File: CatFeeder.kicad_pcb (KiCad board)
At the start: 2 copper layers, 96.3 x 51.8 mm, 49 parts, among them J1 B2B-XH-A(LF)(SN), J10 B2B-XH-A(LF)(SN), J11 B2B-XH-A(LF)(SN), J2 B3B-XH-A(LF)(SN), J3 Barrel_Jack, J4 B4B-XH-A(LF)(SN), J5 Conn_01x08_Female, J6 Conn_01x08_Female, J7 B2B-XH-A(LF)(SN), J8 B2B-XH-A(LF)(SN), J9 B2B-XH-A(LF)(SN), Q1 Q_NPN_BEC, Q2 Q_NPN_BEC, U1 SN74LVC1T45DBV, U2 LM2586SX-ADJ/NOPB_1, U3 DRV8871DDA

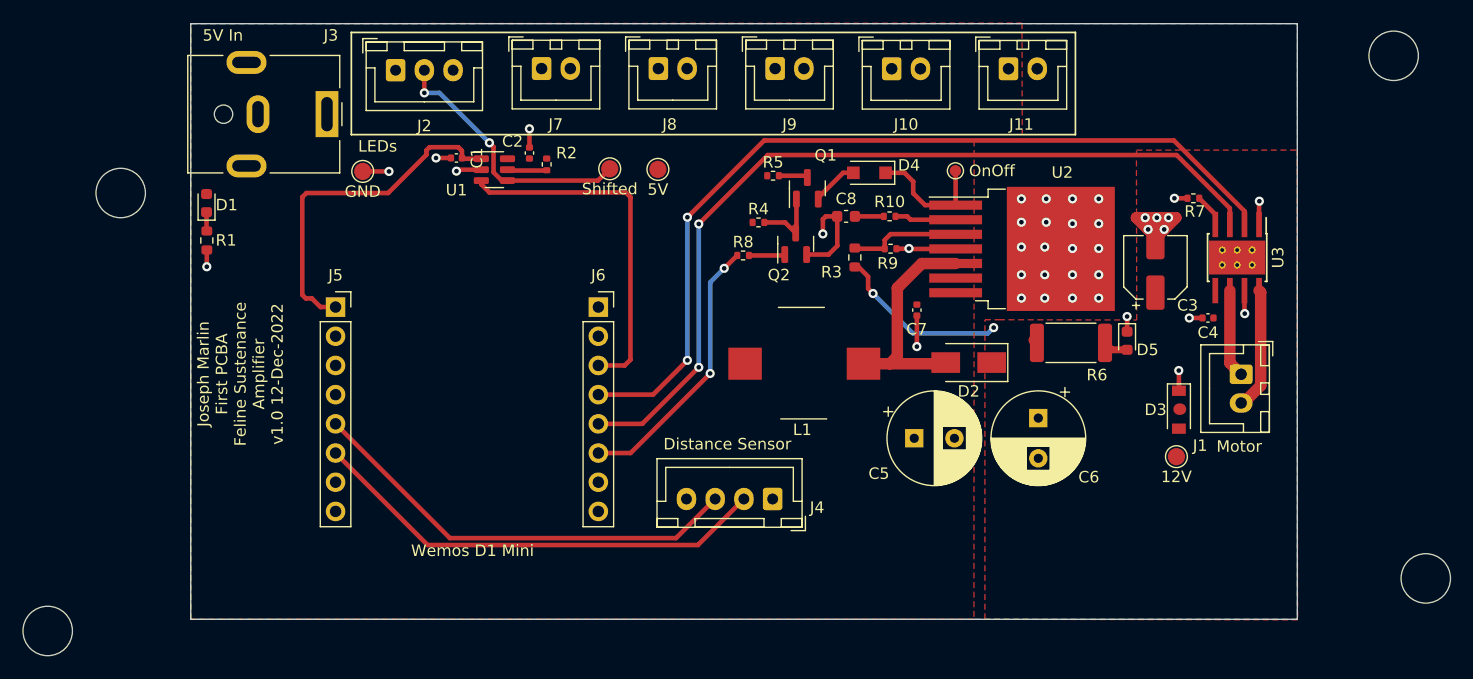
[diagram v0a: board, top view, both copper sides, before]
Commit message: Add pull ups to signals, tweak layout, reduce board size, add mounting holes
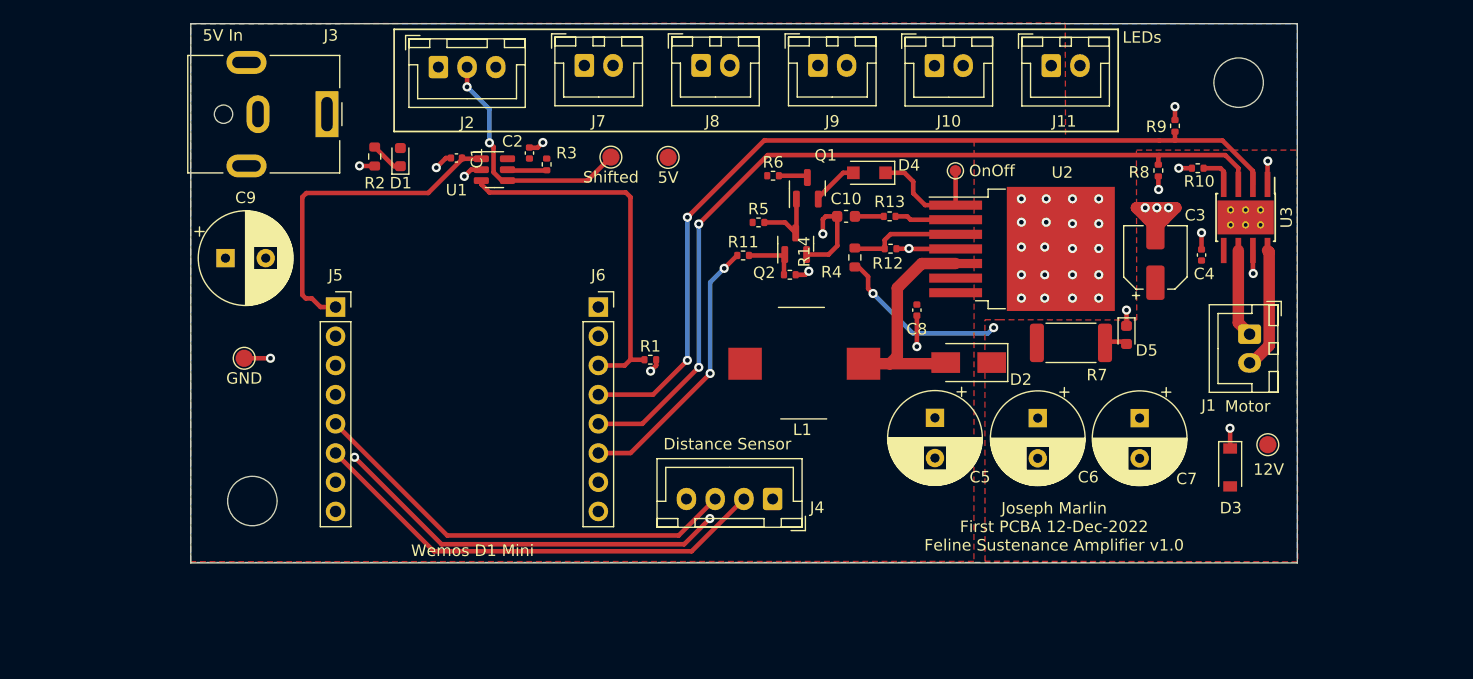
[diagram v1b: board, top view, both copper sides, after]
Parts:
- removed the REF** at (85.1, 120.9)
- removed the REF** at (205.0, 116.3)
- added C7: 680uF 25V, Capacitor_THT:CP_Radial_D8.0mm_P3.50mm, F.Cu at (180.1, 102.4)
- added C9: 100uF 25V, Capacitor_THT:CP_Radial_D8.0mm_P3.50mm, F.Cu at (100.6, 88.5)
- added R1: 30K, Resistor_SMD:R_0402_1005Metric, F.Cu at (137.5, 97.3)
- added R14: 30K, Resistor_SMD:R_0402_1005Metric, F.Cu at (149.7, 89.9)
- added R8: 30K, Resistor_SMD:R_0402_1005Metric, F.Cu at (181.7, 80.8)
- added R9: 30K, Resistor_SMD:R_0402_1005Metric, F.Cu at (183.2, 77.0)
- C6: value 680uF 16V -> 680uF 25V
- moved REF** 29.1 mm to (102.9, 109.6)
- moved TP5 19.3 mm to (102.2, 97.2)
- moved D1 17.3 mm to (115.8, 79.7)
- moved R2 16.3 mm to (113.5, 79.6)
- moved REF** 13.7 mm to (188.7, 73.2)
- moved TP3 8.02 mm to (191.2, 104.7)
- moved D3 6.71 mm to (188.0, 106.7)
- moved C4 5.51 mm to (185.5, 88.2), turned to 90 degrees
- moved J10 3.73 mm to (162.2, 71.7)
- moved J11 3.73 mm to (172.4, 71.7)
- moved J2 3.73 mm to (119.1, 71.8)
- moved J7 3.73 mm to (131.8, 71.7)
- moved J8 3.73 mm to (141.9, 71.7)
- moved J9 3.73 mm to (152.1, 71.7)
- moved J1 3.57 mm to (189.7, 95.1)
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- renumbered C8 to C10, C7 to C8, R7 to R10, R8 to R11, R9 to R12, R10 to R13, R1 to R2, R2 to R3, R3 to R4, R4 to R5, R5 to R6, R6 to R7
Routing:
- net GND: track 44.5 -> 84.0 mm, vias 39 -> 43
- net Net-(Q2-Pad1): track 3.14 -> 4.95 mm
- net /LEDShifted: track 23.0 -> 21.5 mm
- net Net-(D1-Pad1): track 1.65 -> 2.92 mm
- net /LEDCtrl: track 30.9 -> 32.1 mm
- net +3.3V: track 30.2 -> 29.0 mm
- net Net-(D5-Pad2): track 2.50 -> 2.00 mm
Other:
- board size 96.3 x 51.8 mm -> 96.3 x 46.9 mm
- board text added: "Joseph Marlin First PCBA 12-Dec-2022 Feline Sustenance Amplifier v1.0"
- board text removed: "Joseph Marlin First PCBA Feline Sustenance Amplifier v1.0 12-Dec-2022"

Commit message: added series resistor for neopixel control line, layout improvements, changed suspect resistors to 0805 for easier future rework
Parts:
- removed the R5 at (146.9, 85.4)
- added J1: B2B-XH-A(LF)(SN), Connector_JST:JST_XH_B2B-XH-A_1x02_P2.50mm_Vertical, F.Cu at (101.1, 99.6)
- added J8: B2B-XH-A(LF)(SN), Connector_JST:JST_XH_B2B-XH-A_1x02_P2.50mm_Vertical, F.Cu at (190.0, 109.7)
- added R3: 220R, Resistor_SMD:R_0805_2012Metric, F.Cu at (117.6, 78.5)
- added R6: 2.2K, Resistor_SMD:R_0805_2012Metric, F.Cu at (146.3, 84.8)
- R12: renamed from R11; value 10K -> 2.2K; footprint Resistor_SMD:R_0402_1005Metric -> Resistor_SMD:R_0805_2012Metric
- R7: renamed from R6; value 24K -> 22K; footprint Resistor_SMD:R_0402_1005Metric -> Resistor_SMD:R_0805_2012Metric
- moved TP5 53.8 mm to (154.7, 109.0), turned to -90 degrees
- moved TP3 14.0 mm to (181.4, 94.7)
- moved D1 8.76 mm to (114.0, 71.1), turned to -90 degrees
- moved R2 8.76 mm to (111.8, 71.0)
- moved D3 5.89 mm to (188.7, 100.8), turned to 0 degrees
- moved C8 2.59 mm to (163.1, 94.0), turned to 0 degrees
- moved J2 2.59 mm to (187.5, 93.7), turned to 0 degrees
- moved R7 0.62 mm to (147.6, 81.3)
- renumbered J8 to J10, J9 to J11, J10 to J12, J11 to J13, J1 to J2, J2 to J3, J3 to J4, J4 to J5, J5 to J6, J6 to J7, J7 to J9, R9 to R10, R10 to R11, R12 to R13, R13 to R14, R14 to R15, R3 to R4, R4 to R5, R7 to R8, R8 to R9
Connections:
- J3 pad 2: /LEDShifted -> Net-(J3-Pad2)
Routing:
- net Net-(J3-Pad2): track 0.00 -> 8.66 mm, vias 0 -> 1
- net /MtrOutB: track 10.7 -> 6.44 mm
- net /LEDShifted: track 21.5 -> 19.2 mm, vias 2 -> 0
- net /MtrOutA: track 7.69 -> 6.43 mm
- net /MtrCtrlA: track 75.4 -> 76.5 mm
- net Net-(D2-Pad2): track 20.0 -> 21.0 mm
- net Net-(Q1-Pad1): track 6.09 -> 6.97 mm
- net /MtrCtrlB: track 76.4 -> 77.2 mm
- net GND: track 84.0 -> 84.7 mm
- net Net-(D4-Pad2): track 4.07 -> 4.74 mm
- net Net-(D1-Pad1): track 2.92 -> 2.27 mm
- net Net-(Q2-Pad1): track 4.95 -> 4.32 mm
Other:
- board text added: "12V In/Out"
- board text added: "5V In/Out"

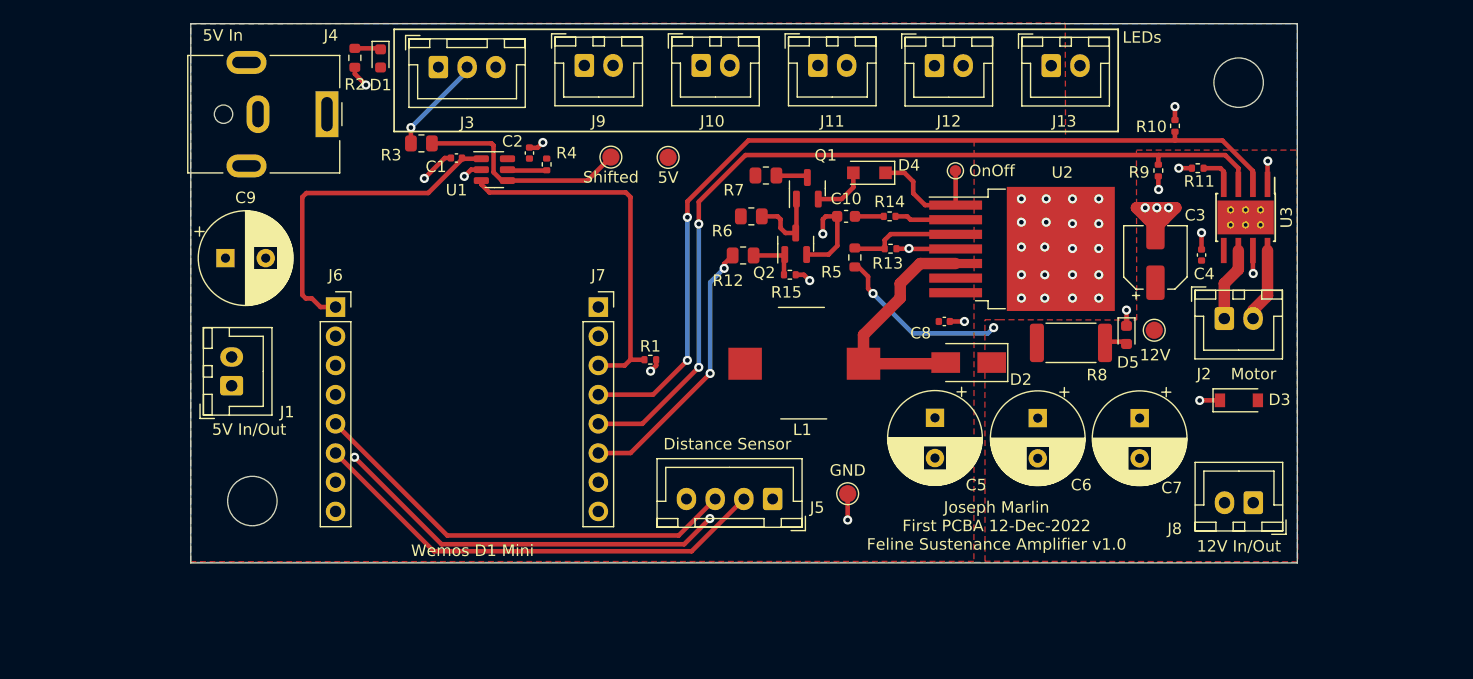
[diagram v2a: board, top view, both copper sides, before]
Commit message: rounded corners, added polarity silkscreen, dimmed the main power LED, fixed polarized cap schematic symbols.
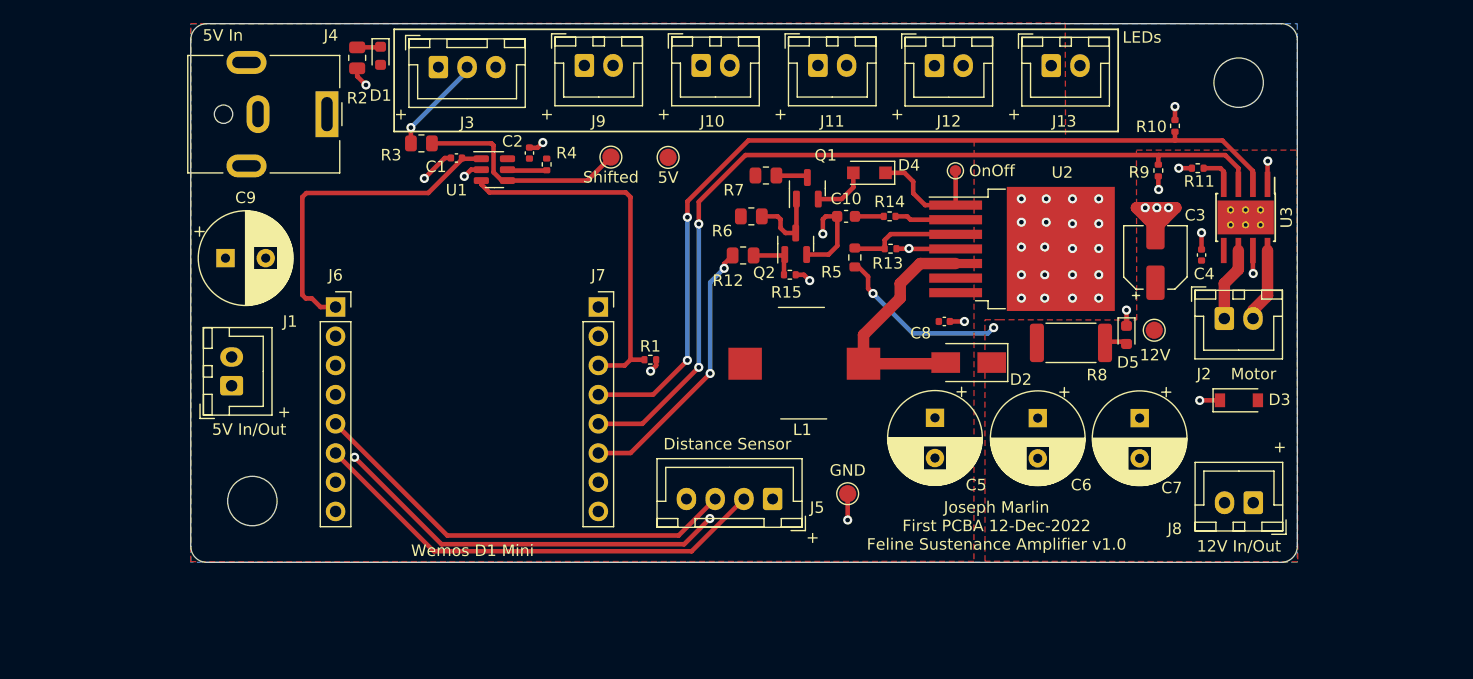
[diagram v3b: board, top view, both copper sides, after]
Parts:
- R2: value 68R 1/10W -> 4.7K; footprint Resistor_SMD:R_0603_1608Metric -> Resistor_SMD:R_0805_2012Metric
- moved D1 0.23 mm to (114.0, 70.9)
- moved R2 0.20 mm to (112.0, 71.0)
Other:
- outline, holes or cut-outs redrawn
- board text added: "+"

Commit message: Manufacturing outputs
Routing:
- net +5V: track 0.00 -> 3.23 mm, vias 0 -> 2
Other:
- board text added: "Joseph Marlin First PCBA 17-Dec-2022 Feline Sustenance Amplifier v1.0"
- board text removed: "Joseph Marlin First PCBA 12-Dec-2022 Feline Sustenance Amplifier v1.0"
